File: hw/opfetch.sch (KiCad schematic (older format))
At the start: 11 parts

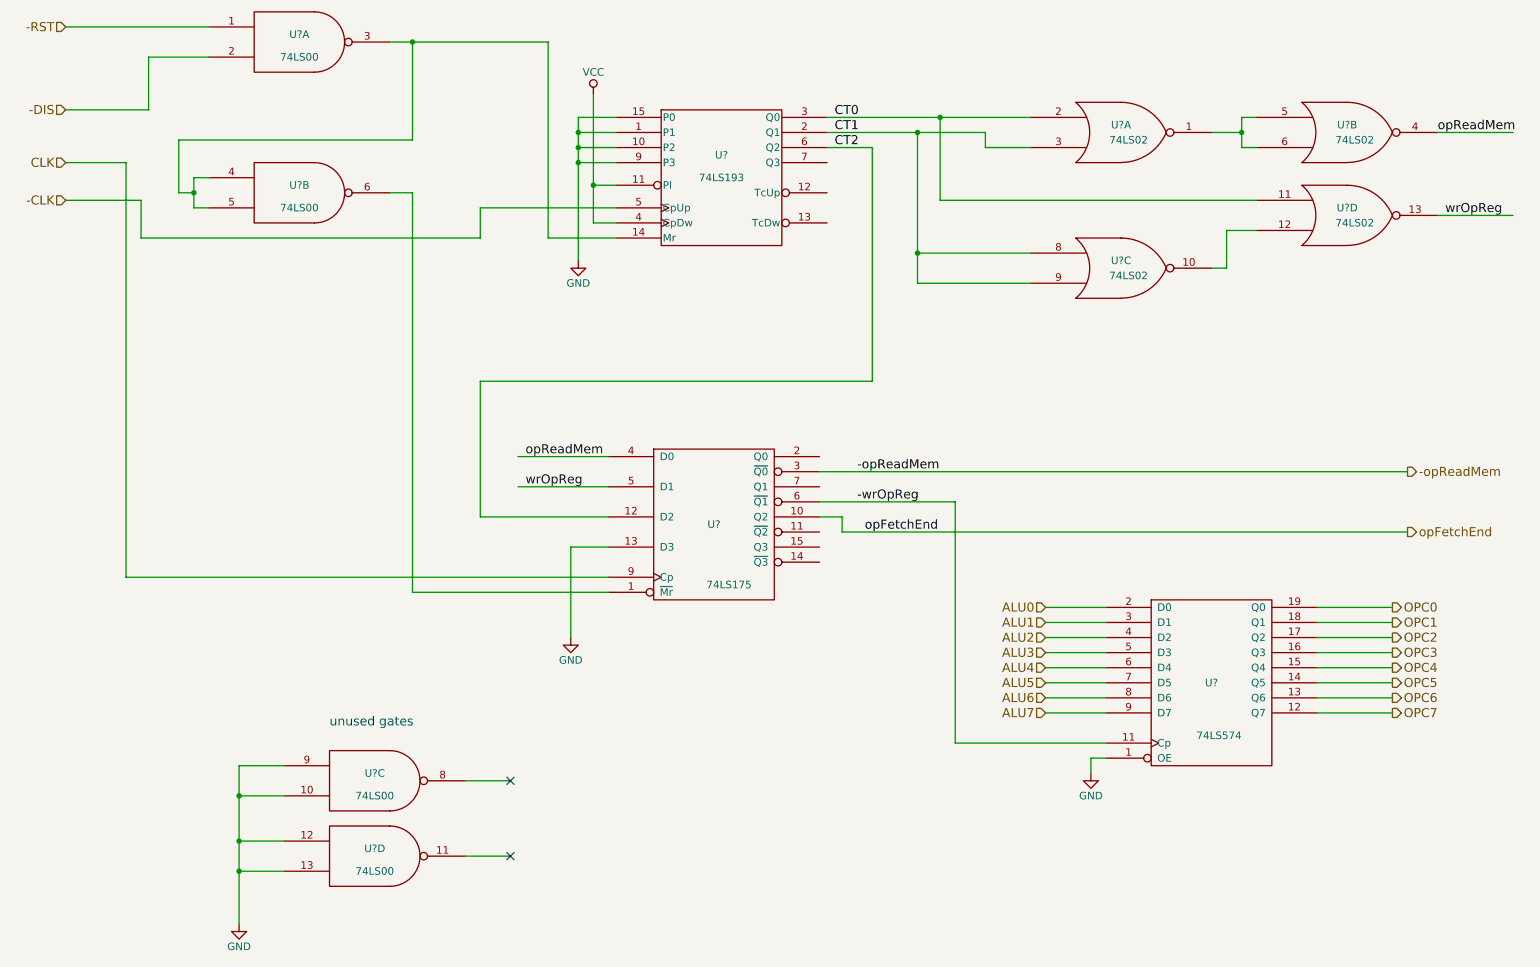
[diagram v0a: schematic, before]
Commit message: clean up opfetch, finishing touches on phase logic
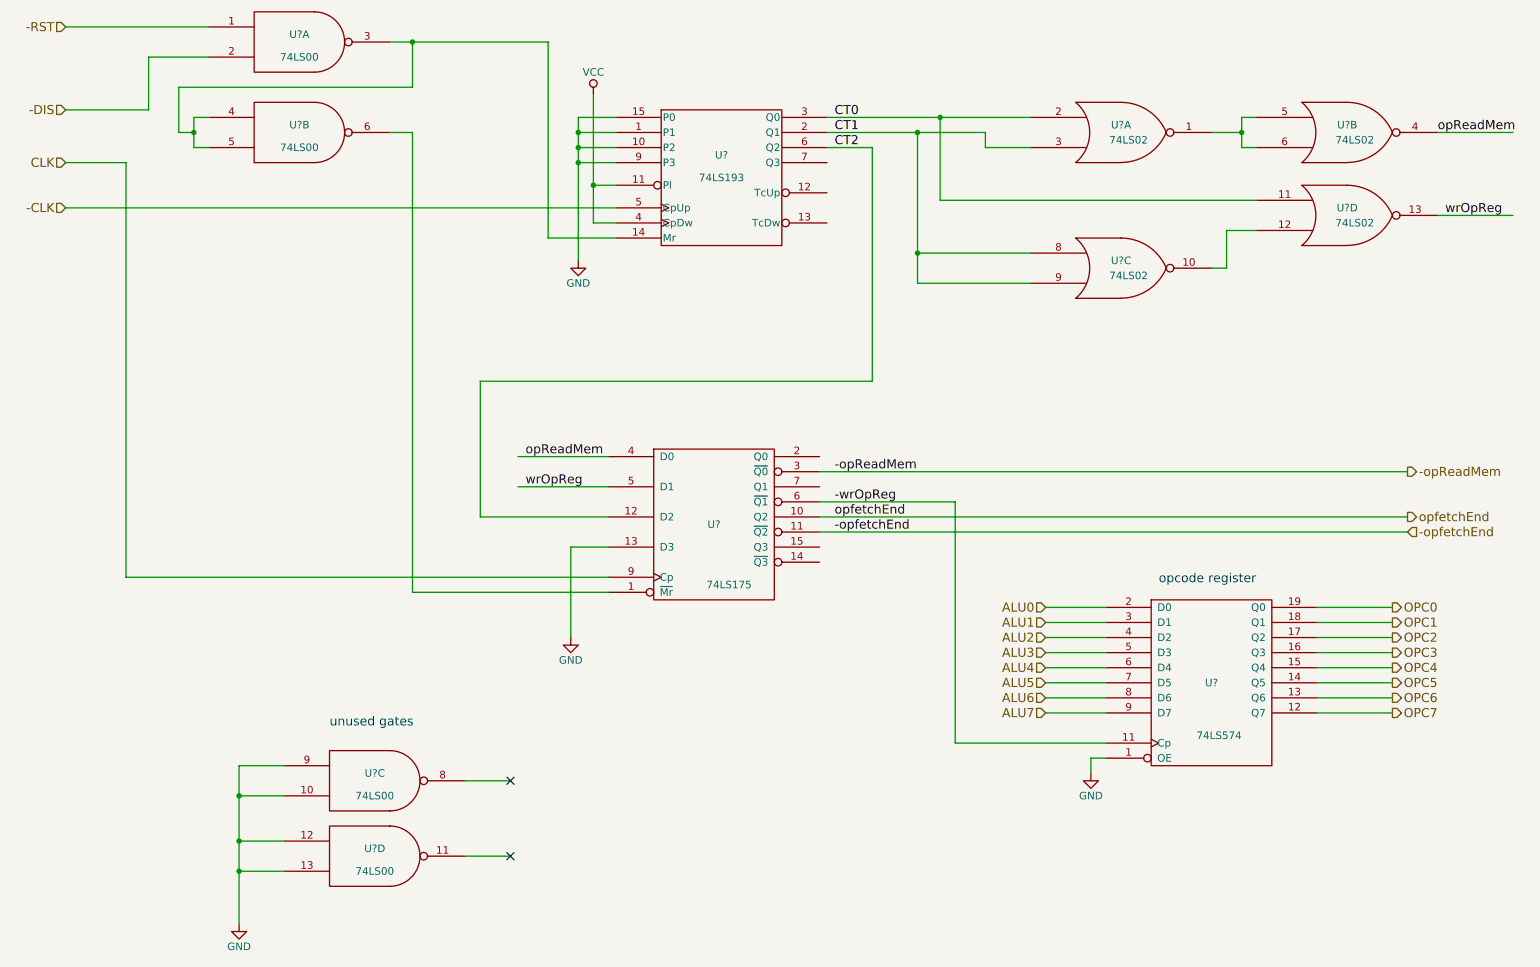
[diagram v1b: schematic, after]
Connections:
- net labels added: -opfetchEnd, opfetchEnd
- net labels removed: opFetchEnd
- wire segments 92 -> 87
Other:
- note added: "opcode register"
- moved on the sheet: U?B
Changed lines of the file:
@@
 Text HLabel 1100 1800 0    60   Input ~ 0
 CLK
-Text HLabel 1100 2050 0    60   Input ~ 0
+Text HLabel 1100 2100 0    60   Input ~ 0
 -CLK
 Text HLabel 1100 1450 0    60   Input ~ 0
@@
 L 74LS00 U?
 U 2 1 59284C82
-P 2650 2000
-F 0 "U?" H 2650 2050 50  0000 C CNN
-F 1 "74LS00" H 2650 1900 50  0000 C CNN
-F 2 "" H 2650 2000 50  0001 C CNN
-F 3 "" H 2650 2000 50  0001 C CNN
-	2    2650 2000
+P 2650 1600
+F 0 "U?" H 2650 1650 50  0000 C CNN
+F 1 "74LS00" H 2650 1500 50  0000 C CNN
+F 2 "" H 2650 1600 50  0001 C CNN
+F 3 "" H 2650 1600 50  0001 C CNN
+	2    2650 1600
 	1    0    0    -1
 $EndComp
@@
 	3250 1000 4300 1000
 Wire Wire Line
-	3400 1000 3400 1650
-Wire Wire Line
-	3400 1650 1850 1650
-Wire Wire Line
-	1850 1650 1850 2000
-Wire Wire Line
-	1850 2000 1950 2000
-Wire Wire Line
-	1950 1900 1950 2100
-Wire Wire Line
-	1950 1900 2050 1900
-Wire Wire Line
-	1950 2100 2050 2100
-Connection ~ 1950 2000
+	1850 1600 1950 1600
+Wire Wire Line
+	1950 1500 1950 1700
+Wire Wire Line
+	1950 1500 2050 1500
+Wire Wire Line
+	1950 1700 2050 1700
+Connection ~ 1950 1600
 Wire Wire Line
 	4750 2300 4300 2300
 Wire Wire Line
 	4300 2300 4300 1000
-Connection ~ 3400 1000
-Wire Wire Line
-	3250 2000 3400 2000
-Wire Wire Line
-	3400 2000 3400 4650
+Wire Wire Line
+	3400 1600 3400 4650
 Wire Wire Line
 	3400 4650 4700 4650
 Wire Wire Line
-	4750 2100 3850 2100
-Wire Wire Line
-	3850 2100 3850 2300
-Wire Wire Line
-	3850 2300 1600 2300
-Wire Wire Line
-	1600 2300 1600 2050
-Wire Wire Line
-	1600 2050 1100 2050
+	1100 2100 4750 2100
 Wire Wire Line
 	1500 4550 4700 4550
@@
 Wire Wire Line
 	6100 4050 7000 4050
-Wire Wire Line
-	6100 4150 6250 4150
-Wire Wire Line
-	6250 4150 6250 4250
-Wire Wire Line
-	6250 4250 10000 4250
-Text Label 6350 3850 0    60   ~ 0
+Text Label 6200 3850 0    60   ~ 0
 -opReadMem
-Text Label 6350 4050 0    60   ~ 0
+Text Label 6200 4050 0    60   ~ 0
 -wrOpReg
-Text Label 6400 4250 0    60   ~ 0
-opFetchEnd
 Text HLabel 10000 3850 2    60   Output ~ 0
 -opReadMem
-Text HLabel 10000 4250 2    60   Output ~ 0
-opFetchEnd
+Text HLabel 10000 4150 2    60   Output ~ 0
+opfetchEnd
 $Comp
 L 74LS574 U?
@@
 Text Notes 2850 5550 0    60   ~ 0
 unused gates
+Text HLabel 10000 4250 2    60   Input ~ 0
+-opfetchEnd
+Wire Wire Line
+	10000 4150 6100 4150
+Wire Wire Line
+	10000 4250 6100 4250
+Wire Wire Line
+	1850 1600 1850 1300
+Wire Wire Line
+	1850 1300 3400 1300
+Wire Wire Line
+	3400 1300 3400 1000
+Connection ~ 3400 1000
+Wire Wire Line
+	3250 1600 3400 1600
+Text Label 6200 4150 0    60   ~ 0
+opfetchEnd
+Text Label 6200 4250 0    60   ~ 0
+-opfetchEnd
+Text Notes 8350 4600 0    60   ~ 0
+opcode register
 $EndSCHEMATC
